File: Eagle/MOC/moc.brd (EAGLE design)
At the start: 100 x 80 mm, 33 parts, among them IC2 74HC595N, IC3 74HC595N, IC4 74HC595N, IC6 MEGA8-P, IC7 7805TV, K1 4052, Q1 20MHz

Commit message: hardware tests, all features
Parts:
- removed C10, C9: (no value), resistor:C025-025X050
- removed C5: (no value), resistor:E2,5-7
- removed C8: 100n, resistor:C025-025X050
- removed IC4: 74HC595N, 74xx-eu:DIL16
- removed L1: (no value), resistor:0207/10
- removed Q1: 20MHz, crystal:HC49/S
- added H1, H2, H3, H4, H5, H6: MOUNT-HOLE3.2, holes:3,2
- added JP10: (no value), pinhead:1X03
- added JP11: (no value), pinhead:1X02/90
- added JP2: HV_MODULE, pinhead:1X02
- added JP3: M_SW, pinhead:1X02/90
- added JP7: H_SW, pinhead:1X02/90
- added JP8: (no value), pinhead:1X08
- added JP9: prog, pinhead:1X03
- C12: device resistor:E2,5-7 -> resistor:E3,5-8
- IC7: value 7805TV -> 7805T; device linear:TO220V -> linear:TO220H
- JP1: device pinhead:1X30 -> pinhead:1X08
- JP4: value (none) -> DS3231_POWER
- JP5: value (none) -> DS3231_SIGNALS
- JP6: value (none) -> RELAY_MODE
- R43: device resistor:0207/7 -> resistor:0207/10
- R44, R45: device resistor:0204/5 -> resistor:0207/10
- R47: device resistor:0204V -> resistor:0207/10
- moved C12 166.4 mm to (100.3, 49.5)
- moved IC7 142.6 mm to (99.1, 27.9)
- moved C7 138.3 mm to (68.6, 20.3)
- moved C14 131.4 mm to (92.7, 12.7), turned to 180 degrees
- moved D2 129.2 mm to (91.4, 41.9), turned to 90 degrees
- moved C13 122.6 mm to (99.1, 43.2)
- moved X1 119.4 mm to (90.2, 54.6)
- moved IC3 113.1 mm to (66.0, 29.2), turned to 180 degrees
- moved R47 112.2 mm to (45.7, 7.62), turned to 180 degrees
- moved C3 104.1 mm to (54.6, 29.2), turned to 270 degrees
- moved JP6 103.4 mm to (64.8, 49.5)
- moved JP1 102.7 mm to (49.5, 55.9), turned to 180 degrees
- moved C11 101.4 mm to (68.6, 7.62), turned to 180 degrees
- moved IC6 100.6 mm to (68.6, 14.0)
- moved R44 97.9 mm to (38.1, 11.4), turned to 90 degrees
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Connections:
- removed net D0: IC4.7, JP1.24
- removed net D1: IC4.6, JP1.23
- removed net D2: IC4.5, JP1.22
- removed net D3: JP1.21
- removed net D4: IC4.3, IC4.4, JP1.20
- removed net D5: IC4.2, JP1.19
- removed net D6: IC4.1, JP1.18
- removed net D7: IC4.15, JP1.17
- removed net HV: JP1.30
- removed net N$41: C9.2, IC6.9, Q1.2
- removed net N$42: C10.2, IC6.10, Q1.1
- removed net N$52: C8.2, IC6.20, L1.1
- removed net N$56: IC6.1, R47.1
- removed net S_IN: IC4.14, IC6.18
- removed net VCC: IC2.10, IC3.10, IC4.10
- new net H_CH: IC6.15, JP7.1
- new net MISO: IC6.18, JP9.2
- new net M_CH: IC6.14, JP3.1
- new net NEON: IC6.13, JP10.3
- new net RESET: IC6.1, JP11.1, R47.1
- net +12V: now also JP2.1
- net +5V: now also IC2.10, IC3.10, IC6.20, JP10.1; no longer C5.+, IC4.16, JP1.26, L1.2
- net D10: now also JP8.6; no longer JP1.14
- net D11: now also JP8.5; no longer JP1.13
- net D12: now also JP8.4; no longer JP1.12
- net D13: now also JP8.3; no longer JP1.11
- net D14: now also JP8.2; no longer JP1.10
- net D15: now also JP8.1; no longer JP1.9
- net D8: now also JP8.8; no longer JP1.16
- net D9: now also JP8.7; no longer JP1.15
- net GND: now also JP10.2, JP11.2, JP2.2, JP3.2, JP7.2; no longer C10.1, C5.-, C8.1, C9.1, IC4.13, IC4.8, JP1.25
- net H_IN: now also IC6.25; no longer IC6.23
- net IN_CLK: now also IC6.24; no longer IC4.11, IC6.17
- net MODE_0: now also IC6.17, JP9.1; no longer IC6.2
- net MODE_1: now also IC6.16; no longer IC6.3
- net M_IN: now also JP9.3
- net OUT_CLK: now also IC6.23; no longer IC4.12, IC6.16
- net RELAY: now also IC6.2; no longer IC6.26
- net SQW: now also IC6.26; no longer IC6.24
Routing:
- net GND: track 0.00 -> 353.3 mm
- net +5V: track 0.00 -> 228.7 mm, vias 0 -> 8
- net +12V: track 0.00 -> 174.5 mm, vias 0 -> 2
- net IN_CLK: track 0.00 -> 47.0 mm, vias 0 -> 2
- net MODE_0: track 0.00 -> 43.5 mm
- net OUT_CLK: track 0.00 -> 42.7 mm, vias 0 -> 2
- net M_CH: track 0.00 -> 42.3 mm, vias 0 -> 2
- net MODE_1: track 0.00 -> 38.7 mm
- net N$53: track 0.00 -> 38.2 mm, vias 0 -> 2
- net H_CH: track 0.00 -> 36.5 mm
- net RESET: track 0.00 -> 33.1 mm, vias 0 -> 2
- net H_IN: track 0.00 -> 29.1 mm
- net SDA: track 0.00 -> 26.5 mm
- net RELAY: track 0.00 -> 21.9 mm
- net D23: track 0.00 -> 14.8 mm
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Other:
- board size 100 x 80 mm -> 134.3 x 58.4 mm

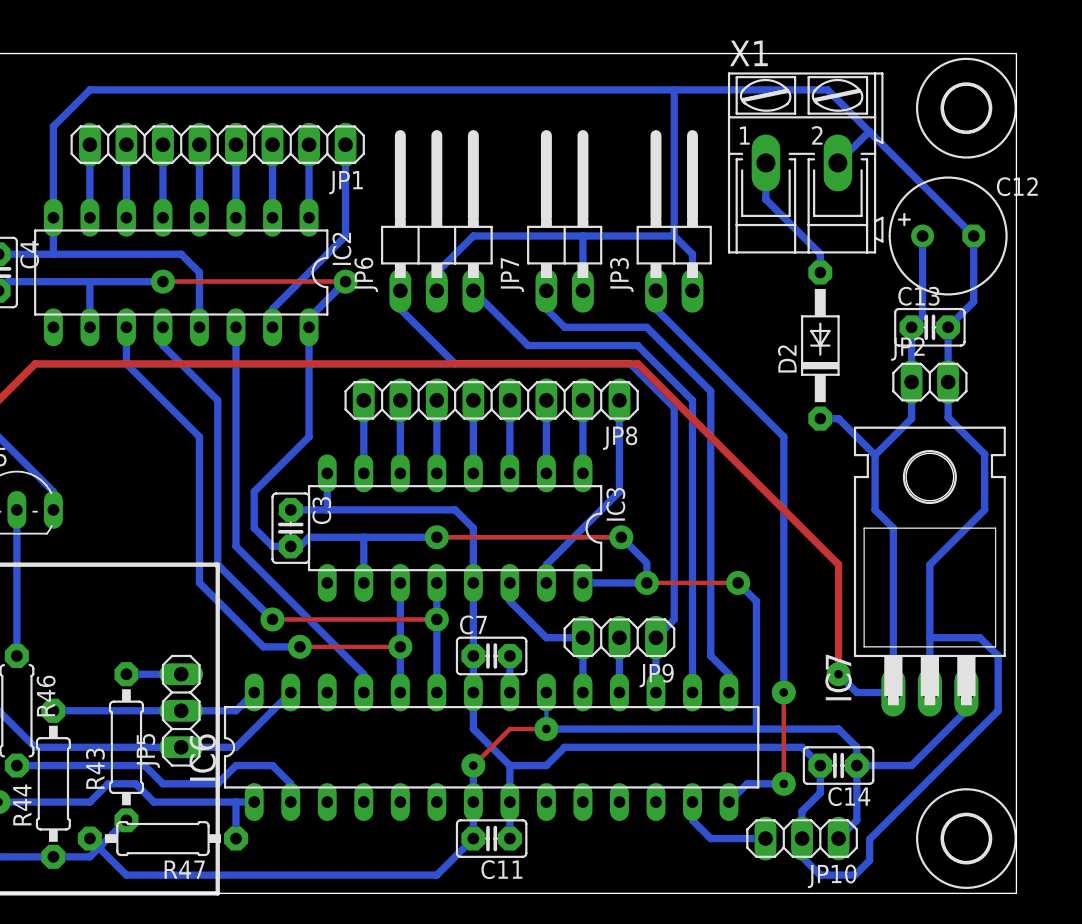
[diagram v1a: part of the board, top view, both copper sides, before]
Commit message: cathodes heat on mode, relay parameters
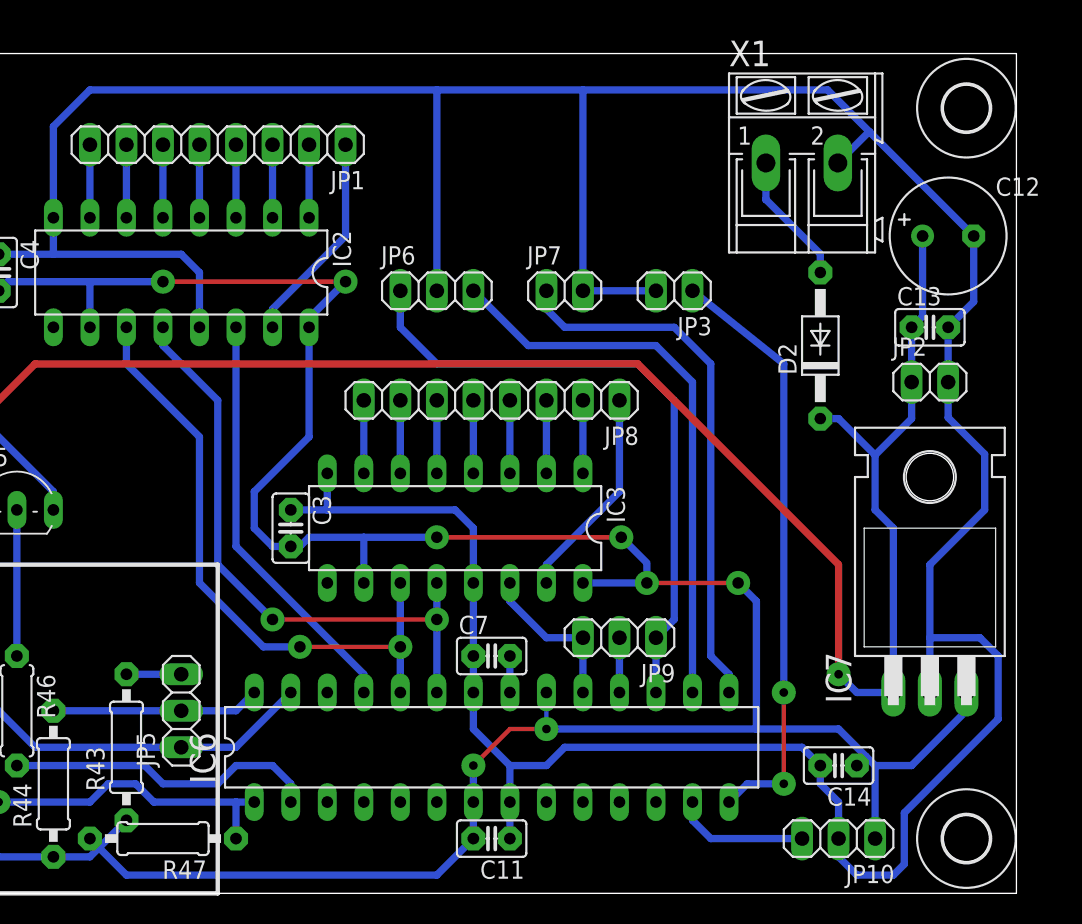
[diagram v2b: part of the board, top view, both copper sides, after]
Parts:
- JP3, JP7: device pinhead:1X02/90 -> pinhead:1X02
- JP6: device pinhead:1X03/90 -> pinhead:1X03
- moved JP3 3.81 mm to (81.3, 45.7), turned to 180 degrees
- moved JP6 3.81 mm to (64.8, 45.7)
- moved JP7 3.81 mm to (73.7, 45.7)
- moved JP10 2.54 mm to (92.7, 7.62)
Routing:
- net GND: track 353.3 -> 347.0 mm
- net NEON: track 6.88 -> 9.42 mm
- net H_CH: track 36.5 -> 37.7 mm
- net MODE_0: track 43.5 -> 44.5 mm
- net MODE_1: track 38.7 -> 39.5 mm
- net M_CH: track 42.3 -> 41.7 mm
